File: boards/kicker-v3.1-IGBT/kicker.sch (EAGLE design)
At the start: 134 parts, among them J1 B2PS-VH(LF)(SN), J2 HFW8R-1ST, J3 B2PS-VH(LF)(SN), J4 B2PS-VH(LF)(SN), J5 2-PIN_2MM-H, J6 3-PIN_2MM-H, J7 !BTN_KCK_PRE_EXT, J8 !BTN_CHP_PRE_EXT, J9 !BTN_CHG_PRE_EXT, Q1 ATP302ATPAK, Q10 BSS806NSOT-23-3, Q2 IRFS4227, Q3 BSS127, Q4 BSS127, Q5 BSS127, Q6 BSS127, Q7 AOD1N60, U1 R-78E5.0-0.5, U2 15V, U3 LT3751FE, U4 AT32ATQFP44, U5 IX4427N, U6 MAX6817, U7 MAX6817

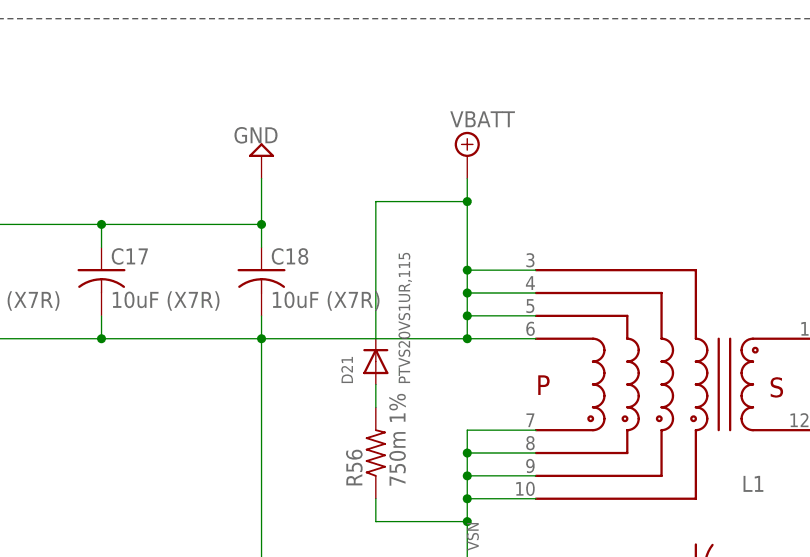
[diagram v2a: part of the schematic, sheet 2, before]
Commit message: Revert "Changed TVS Diode"
This reverts commit 859410941ee6306b805c1c3f21250df0eea6f1d1.
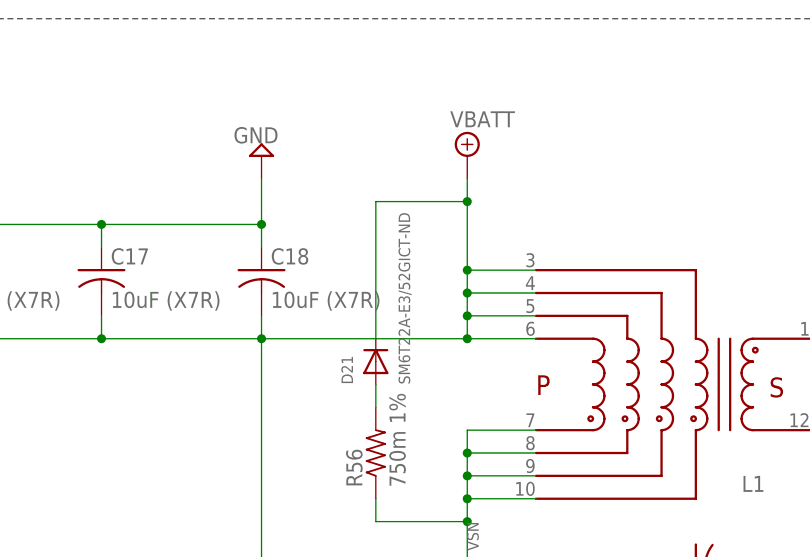
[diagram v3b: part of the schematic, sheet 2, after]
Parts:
- D21: value PTVS20VS1UR,115 -> SM6T22A-E3/52GICT-ND
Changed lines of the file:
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@@
 <grid distance="0.1" unitdist="inch" unit="inch" style="lines" multiple="1" display="no" altdistance="0.01" altunitdist="inch" altunit="inch"/>
 <layers>
-<layer number="1" name="Top" color="4" fill="1" visible="no" active="no"/>
-<layer number="2" name="Route2" color="1" fill="3" visible="no" active="no"/>
-<layer number="3" name="Route3" color="4" fill="3" visible="no" active="no"/>
-<layer number="4" name="Route4" color="1" fill="4" visible="no" active="no"/>
-<layer number="5" name="Route5" color="4" fill="4" visible="no" active="no"/>
-<layer number="6" name="Route6" color="1" fill="8" visible="no" active="no"/>
-<layer number="7" name="Route7" color="4" fill="8" visible="no" active="no"/>
-<layer number="8" name="Route8" color="1" fill="2" visible="no" active="no"/>
-<layer number="9" name="Route9" color="4" fill="2" visible="no" active="no"/>
-<layer number="10" name="Route10" color="1" fill="7" visible="no" active="no"/>
-<layer number="11" name="Route11" color="4" fill="7" visible="no" active="no"/>
-<layer number="12" name="Route12" color="1" fill="5" visible="no" active="no"/>
-<layer number="13" name="Route13" color="4" fill="5" visible="no" active="no"/>
-<layer number="14" name="Route14" color="1" fill="6" visible="no" active="no"/>
-<layer number="15" name="Route15" color="4" fill="6" visible="no" active="no"/>
-<layer number="16" name="Bottom" color="1" fill="1" visible="no" active="no"/>
-<layer number="17" name="Pads" color="2" fill="1" visible="no" active="no"/>
-<layer number="18" name="Vias" color="2" fill="1" visible="no" active="no"/>
-<layer number="19" name="Unrouted" color="6" fill="1" visible="no" active="no"/>
-<layer number="20" name="Dimension" color="15" fill="1" visible="no" active="no"/>
-<layer number="21" name="tPlace" color="7" fill="1" visible="no" active="no"/>
-<layer number="22" name="bPlace" color="7" fill="1" visible="no" active="no"/>
-<layer number="23" name="tOrigins" color="15" fill="1" visible="no" active="no"/>
-<layer number="24" name="bOrigins" color="15" fill="1" visible="no" active="no"/>
-<layer number="25" name="tNames" color="7" fill="1" visible="no" active="no"/>
-<layer number="26" name="bNames" color="7" fill="1" visible="no" active="no"/>
-<layer number="27" name="tValues" color="7" fill="1" visible="no" active="no"/>
-<layer number="28" name="bValues" color="7" fill="1" visible="no" active="no"/>
+<layer number="1" name="Top" color="4" fill="1" visible="yes" active="no"/>
+<layer number="2" name="Route2" color="1" fill="3" visible="yes" active="no"/>
+<layer number="3" name="Route3" color="4" fill="3" visible="yes" active="no"/>
+<layer number="4" name="Route4" color="1" fill="4" visible="yes" active="no"/>
+<layer number="5" name="Route5" color="4" fill="4" visible="yes" active="no"/>
+<layer number="6" name="Route6" color="1" fill="8" visible="yes" active="no"/>
+<layer number="7" name="Route7" color="4" fill="8" visible="yes" active="no"/>
+<layer number="8" name="Route8" color="1" fill="2" visible="yes" active="no"/>
+<layer number="9" name="Route9" color="4" fill="2" visible="yes" active="no"/>
+<layer number="10" name="Route10" color="1" fill="7" visible="yes" active="no"/>
+<layer number="11" name="Route11" color="4" fill="7" visible="yes" active="no"/>
+<layer number="12" name="Route12" color="1" fill="5" visible="yes" active="no"/>
+<layer number="13" name="Route13" color="4" fill="5" visible="yes" active="no"/>
+<layer number="14" name="Route14" color="1" fill="6" visible="yes" active="no"/>
+<layer number="15" name="Route15" color="4" fill="6" visible="yes" active="no"/>
+<layer number="16" name="Bottom" color="1" fill="1" visible="yes" active="no"/>
+<layer number="17" name="Pads" color="2" fill="1" visible="yes" active="no"/>
+<layer number="18" name="Vias" color="2" fill="1" visible="yes" active="no"/>
+<layer number="19" name="Unrouted" color="6" fill="1" visible="yes" active="no"/>
+<layer number="20" name="Dimension" color="15" fill="1" visible="yes" active="no"/>
+<layer number="21" name="tPlace" color="7" fill="1" visible="yes" active="no"/>
+<layer number="22" name="bPlace" color="7" fill="1" visible="yes" active="no"/>
+<layer number="23" name="tOrigins" color="15" fill="1" visible="yes" active="no"/>
+<layer number="24" name="bOrigins" color="15" fill="1" visible="yes" active="no"/>
+<layer number="25" name="tNames" color="7" fill="1" visible="yes" active="no"/>
+<layer number="26" name="bNames" color="7" fill="1" visible="yes" active="no"/>
+<layer number="27" name="tValues" color="7" fill="1" visible="yes" active="no"/>
+<layer number="28" name="bValues" color="7" fill="1" visible="yes" active="no"/>
 <layer number="29" name="tStop" color="7" fill="3" visible="no" active="no"/>
 <layer number="30" name="bStop" color="7" fill="6" visible="no" active="no"/>
@@
 <layer number="35" name="tGlue" color="7" fill="4" visible="no" active="no"/>
 <layer number="36" name="bGlue" color="7" fill="5" visible="no" active="no"/>
-<layer number="37" name="tTest" color="7" fill="1" visible="no" active="no"/>
-<layer number="38" name="bTest" color="7" fill="1" visible="no" active="no"/>
+<layer number="37" name="tTest" color="7" fill="1" visible="yes" active="no"/>
+<layer number="38" name="bTest" color="7" fill="1" visible="yes" active="no"/>
 <layer number="39" name="tKeepout" color="4" fill="11" visible="no" active="no"/>
 <layer number="40" name="bKeepout" color="1" fill="11" visible="no" active="no"/>
@@
 <layer number="44" name="Drills" color="7" fill="1" visible="no" active="no"/>
 <layer number="45" name="Holes" color="7" fill="1" visible="no" active="no"/>
-<layer number="46" name="Milling" color="3" fill="1" visible="no" active="no"/>
-<layer number="47" name="Measures" color="7" fill="1" visible="no" active="no"/>
-<layer number="48" name="Document" color="7" fill="1" visible="no" active="no"/>
-<layer number="49" name="Reference" color="7" fill="1" visible="no" active="no"/>
-<layer number="50" name="dxf" color="7" fill="1" visible="no" active="no"/>
-<layer number="51" name="tDocu" color="7" fill="1" visible="no" active="no"/>
-<layer number="52" name="bDocu" color="7" fill="1" visible="no" active="no"/>
-<layer number="53" name="tGND_GNDA" color="7" fill="9" visible="no" active="no"/>
-<layer number="54" name="bGND_GNDA" color="1" fill="9" visible="no" active="no"/>
-<layer number="56" name="wert" color="7" fill="1" visible="no" active="no"/>
-<layer number="57" name="tCAD" color="7" fill="1" visible="no" active="no"/>
-<layer number="59" name="tCarbon" color="7" fill="1" visible="no" active="no"/>
-<layer number="60" name="bCarbon" color="7" fill="1" visible="no" active="no"/>
+<layer number="46" name="Milling" color="3" fill="1" visible="yes" active="no"/>
+<layer number="47" name="Measures" color="7" fill="1" visible="yes" active="no"/>
+<layer number="48" name="Document" color="7" fill="1" visible="yes" active="no"/>
+<layer number="49" name="Reference" color="7" fill="1" visible="yes" active="no"/>
+<layer number="50" name="dxf" color="7" fill="1" visible="yes" active="no"/>
+<layer number="51" name="tDocu" color="7" fill="1" visible="yes" active="no"/>
+<layer number="52" name="bDocu" color="7" fill="1" visible="yes" active="no"/>
+<layer number="53" name="tGND_GNDA" color="7" fill="9" visible="yes" active="no"/>
+<layer number="54" name="bGND_GNDA" color="1" fill="9" visible="yes" active="no"/>
+<layer number="56" name="wert" color="7" fill="1" visible="yes" active="no"/>
+<layer number="57" name="tCAD" color="7" fill="1" visible="yes" active="no"/>
+<layer number="59" name="tCarbon" color="7" fill="1" visible="yes" active="no"/>
+<layer number="60" name="bCarbon" color="7" fill="1" visible="yes" active="no"/>
 <layer number="90" name="Modules" color="5" fill="1" visible="yes" active="yes"/>
 <layer number="91" name="Nets" color="2" fill="1" visible="yes" active="yes"/>
@@
 <part name="U$6" library="RoboJackets-Discrete" deviceset="IXGK400N30A3" device=""/>
 <part name="U$7" library="RoboJackets-Discrete" deviceset="IXGK400N30A3" device=""/>
-<part name="D21" library="adafruit" deviceset="DIODE" device="SOD-123" value="PTVS20VS1UR,115 "/>
+<part name="D21" library="adafruit" deviceset="DIODE" device="SOD-123" value="SM6T22A-E3/52GICT-ND"/>
 <part name="R56" library="resistor" library_urn="urn:adsk.eagle:library:348" deviceset="R-US_" device="M0805" package3d_urn="urn:adsk.eagle:package:26079/1" value="750m 1%"/>
 <part name="SUPPLY12" library="supply2" library_urn="urn:adsk.eagle:library:372" deviceset="+5V" device=""/>

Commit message: Minor Fixes
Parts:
- D21: value SM6T22A-E3/52GICT-ND -> 1727-5865-1-ND; device adafruit:DIODESOD-123 -> RoboJackets-Diodes:TVS

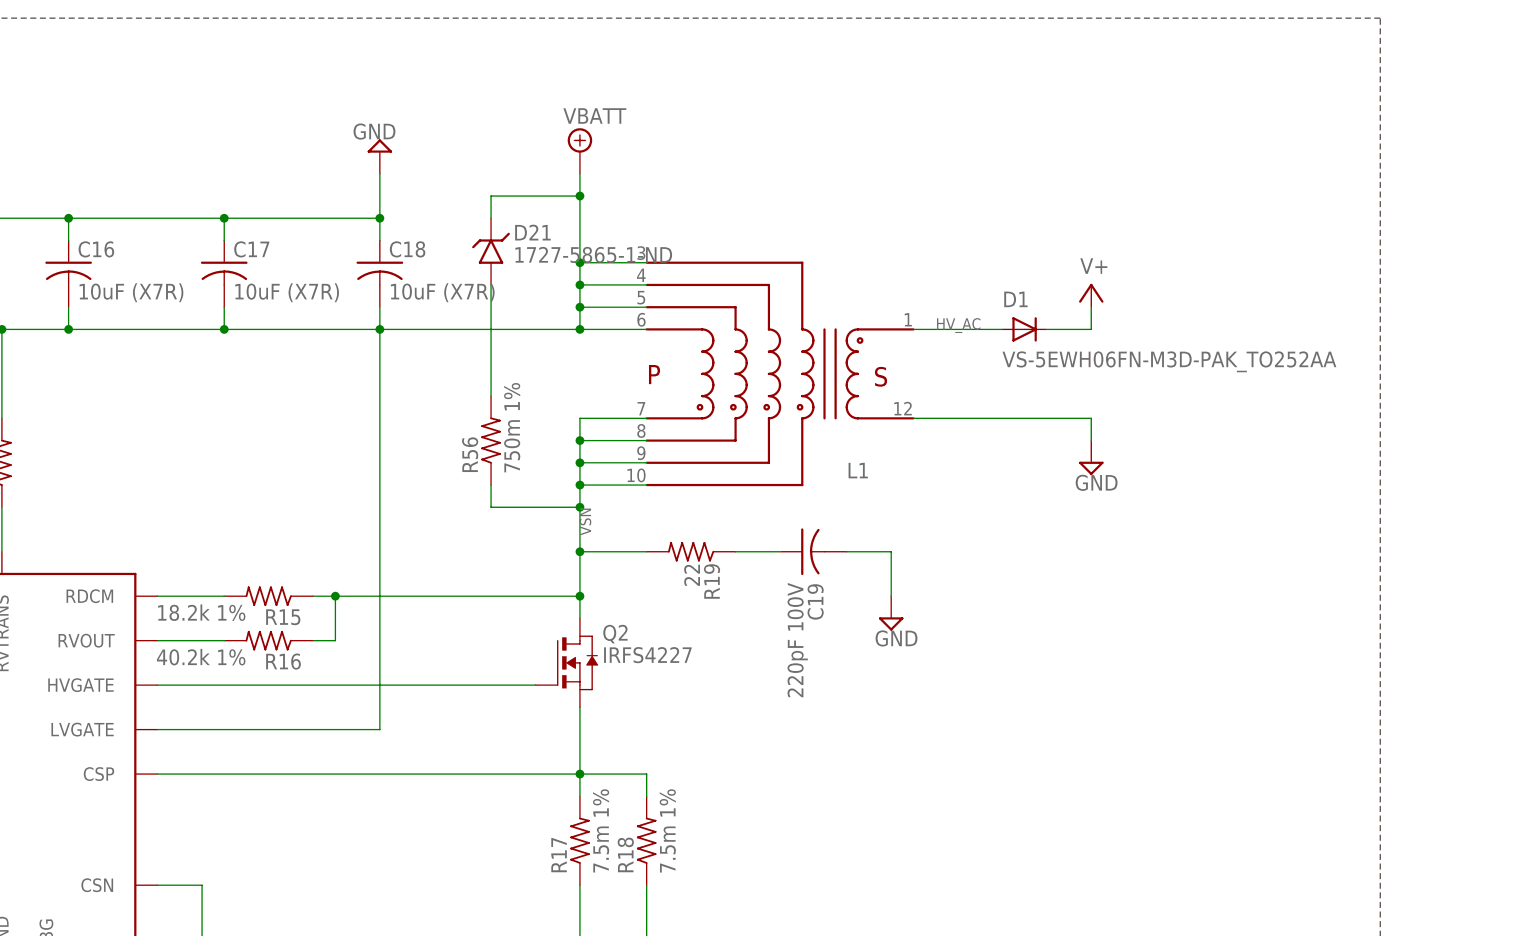
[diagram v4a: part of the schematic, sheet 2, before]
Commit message: Routing/TVS Snubber Fixes
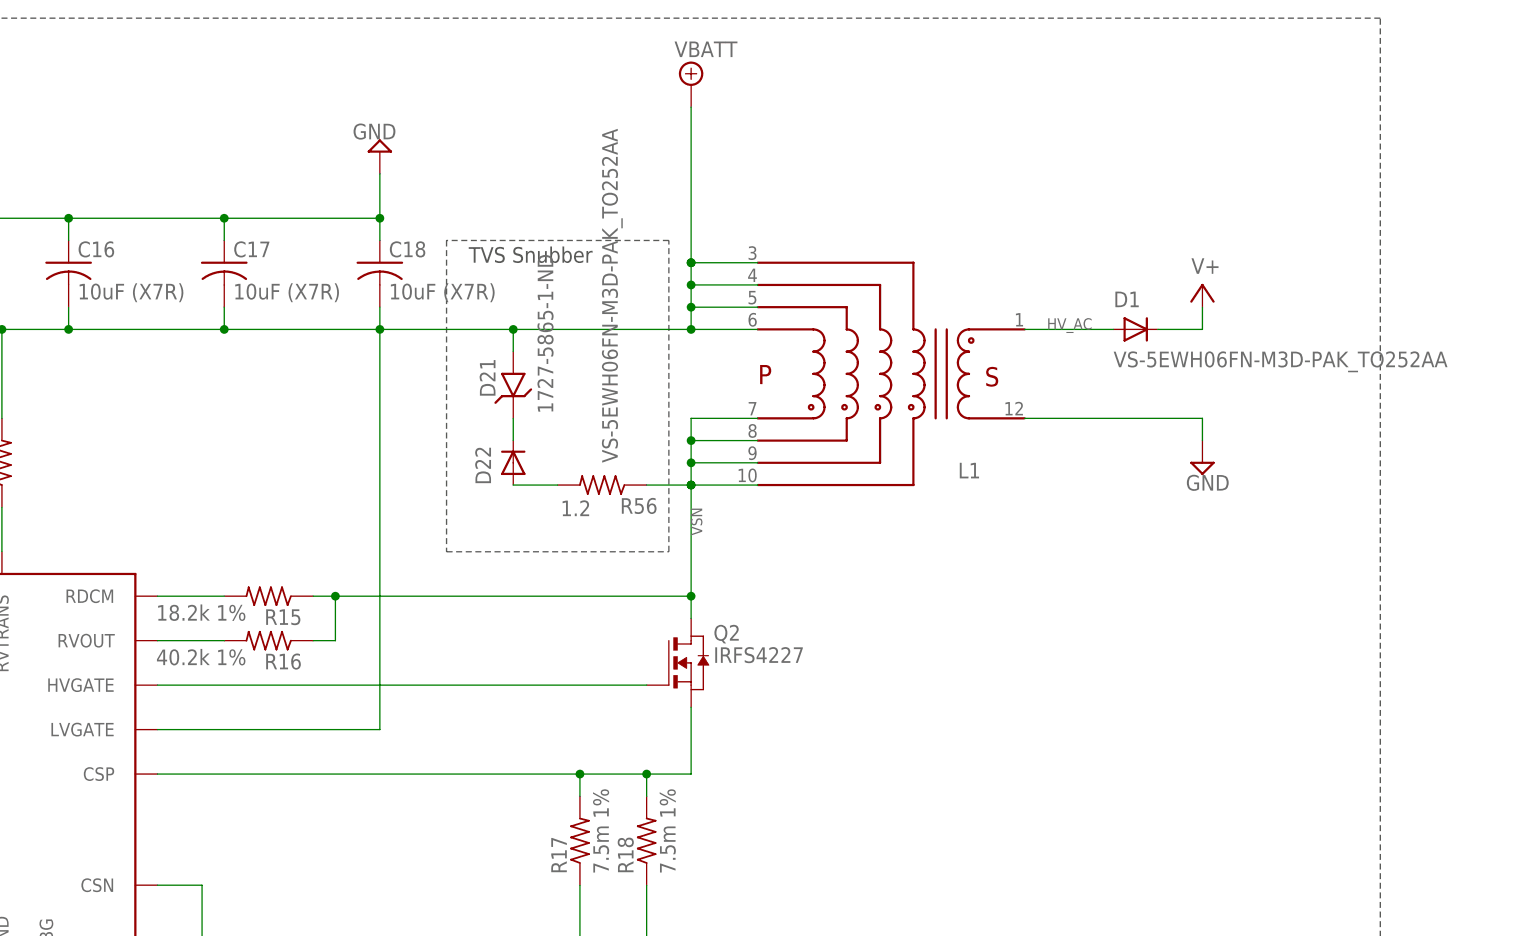
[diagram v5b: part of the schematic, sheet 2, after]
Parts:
- removed C19: 220pF 100V, rcl:C-USC0603
- removed R19: 22, rcl:R-US_R0805
- added D22: VS-5EWH06FN-M3D-PAK_TO252AA, RoboJackets-Diodes:VS-5EWH06FN-M3D-PAK_TO252AA
- D21: value 1727-5865-1-ND -> 1727-5865-1-ND; device RoboJackets-Diodes:TVS -> RoboJackets-Diodes:TVSSOD123W
- R56: value 750m 1% -> 1.2
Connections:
- removed net N$32: C19.1, R19.1
- new net N$18: D22.A, R56.2
- net GND: no longer C19.2
- net N$23: now also D21.C, D22.C; no longer D21.A, R56.2
- net VBATT: now also D21.A; no longer D21.C
- net VSN: no longer R19.2
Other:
- note added: "TVS Snubber"
- moved on the sheet: D1, D21, L1, Q2, R56
